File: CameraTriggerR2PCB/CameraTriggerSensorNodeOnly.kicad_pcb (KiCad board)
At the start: 2 copper layers, 73.7 x 100.3 mm, 44 parts, among them IC1 3178, J1 Power, J13 +5V Always on, J13 Serial, J14 Ext power switch, J2 Qwiic_Connector, J3 Aux out, J4 HighLowIn, J5 Laser, J6 Sensor, Q1 PN2222A, SW1 AS11CB, SW3 SW_Poll, U1 LM7805_TO220

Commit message: Add files via upload
Adding LightSensor2
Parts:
- moved H1 1.27 mm to (153.7, 127.0)
- moved H4 1.27 mm to (90.2, 127.0)
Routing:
- net +3V3: track 180.6 -> 174.4 mm
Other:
- board size 73.7 x 100.3 mm -> 73.7 x 99.1 mm
- board text added: "+3.3V"
- board text added: "+5V"
- board text added: "Gnd"
- board text added: "Sensor"
- board text removed: "+3.3"
- board text removed: "SIG"
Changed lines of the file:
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@@
   (general
     (thickness 1.6)
-    (drawings 26)
-    (tracks 262)
+    (drawings 24)
+    (tracks 261)
     (zones 0)
     (modules 44)
@@
   )
   (module MountingHole:MountingHole_3.7mm_Pad (layer F.Cu)
-    (at 90.17 128.27 270)
+    (at 90.17 127 270)
     (descr "Mounting Hole 3.7mm")
     (tags "mounting hole 3.7mm")
@@
   )
   (module MountingHole:MountingHole_3.7mm_Pad (layer F.Cu)
-    (at 153.67 128.27 270)
+    (at 153.67 127 270)
     (descr "Mounting Hole 3.7mm")
     (tags "mounting hole 3.7mm")
@@
     )
   )
-  (gr_text +5 (at 92.71 81.28) (layer F.Cu)
-    (effects (font (size 1.5 1.5) (thickness 0.3)))
-  )
-  (gr_text Rx (at 97.79 86.36) (layer F.Cu)
-    (effects (font (size 1.5 1.5) (thickness 0.3)))
-  )
-  (gr_text Tx (at 97.79 91.44) (layer F.Cu)
-    (effects (font (size 1.5 1.5) (thickness 0.3)))
-  )
-  (gr_text G (at 92.71 96.52) (layer F.Cu)
-    (effects (font (size 1.5 1.5) (thickness 0.3)))
-  )
-  (gr_text Signal (at 100.33 116.84) (layer F.Cu)
-    (effects (font (size 1.5 1.5) (thickness 0.3)))
-  )
-  (gr_text +3.3 (at 99.06 121.92) (layer F.Cu)
-    (effects (font (size 1.5 1.5) (thickness 0.3)))
-  )
-  (gr_text G (at 97.79 114.3) (layer F.Cu)
-    (effects (font (size 1.5 1.5) (thickness 0.3)))
-  )
-  (gr_text G (at 114.3 44.45) (layer F.Cu)
-    (effects (font (size 1.5 1.5) (thickness 0.3)))
-  )
-  (gr_text +5 (at 118.11 44.45) (layer F.Cu)
-    (effects (font (size 1.5 1.5) (thickness 0.3)))
-  )
-  (gr_text G (at 144.78 96.52) (layer F.Cu)
-    (effects (font (size 1.5 1.5) (thickness 0.3)))
-  )
-  (gr_text +5 (at 143.51 93.98) (layer F.Cu)
-    (effects (font (size 1.5 1.5) (thickness 0.3)))
-  )
-  (gr_text +3.3 (at 135.89 104.14) (layer F.Cu)
-    (effects (font (size 1.5 1.5) (thickness 0.3)))
-  )
-  (gr_text G (at 137.16 110.49) (layer F.Cu)
-    (effects (font (size 1.5 1.5) (thickness 0.3)))
-  )
-  (gr_text SIG (at 137.16 106.68) (layer F.Cu)
-    (effects (font (size 1.5 1.5) (thickness 0.3)))
-  )
-  (gr_text SIG (at 146.05 116.84) (layer F.Cu)
-    (effects (font (size 1.5 1.5) (thickness 0.3)))
-  )
-  (gr_text G (at 147.32 119.38) (layer F.Cu)
-    (effects (font (size 1.5 1.5) (thickness 0.3)))
-  )
+  (gr_text Gnd (at 114.3 41.91) (layer Dwgs.User)
+    (effects (font (size 1 1) (thickness 0.15)))
+  )
+  (gr_text +5V (at 118.11 41.91) (layer Dwgs.User)
+    (effects (font (size 1 1) (thickness 0.15)))
+  )
+  (gr_text G (at 95.25 96.52) (layer Dwgs.User)
+    (effects (font (size 1 1) (thickness 0.15)))
+  )
+  (gr_text +5 (at 91.44 81.28) (layer Dwgs.User)
+    (effects (font (size 1 1) (thickness 0.15)))
+  )
+  (gr_text Rx (at 96.52 86.36) (layer Dwgs.User)
+    (effects (font (size 1 1) (thickness 0.15)))
+  )
+  (gr_text Tx (at 99.06 92.71) (layer Dwgs.User)
+    (effects (font (size 1 1) (thickness 0.15)))
+  )
+  (gr_text Gnd (at 144.78 96.52) (layer Dwgs.User)
+    (effects (font (size 1 1) (thickness 0.15)))
+  )
+  (gr_text +5V (at 144.78 93.98) (layer Dwgs.User)
+    (effects (font (size 1 1) (thickness 0.15)))
+  )
+  (gr_text Gnd (at 137.16 109.22) (layer Dwgs.User)
+    (effects (font (size 1 1) (thickness 0.15)))
+  )
+  (gr_text Sensor (at 137.16 106.68) (layer Dwgs.User)
+    (effects (font (size 1 1) (thickness 0.15)))
+  )
+  (gr_text +3.3V (at 135.89 104.14) (layer Dwgs.User)
+    (effects (font (size 1 1) (thickness 0.15)))
+  )
+  (gr_text Gnd (at 146.05 119.38) (layer Dwgs.User)
+    (effects (font (size 1 1) (thickness 0.15)))
+  )
+  (gr_text Signal (at 147.32 115.57) (layer Dwgs.User)
+    (effects (font (size 1 1) (thickness 0.15)))
+  )
+  (gr_text Sensor (at 97.79 116.84) (layer Dwgs.User)
+    (effects (font (size 1 1) (thickness 0.15)))
+  )
+  (gr_text +3.3V (at 97.79 121.92) (layer Dwgs.User)
+    (effects (font (size 1 1) (thickness 0.15)))
+  )
+  (gr_text Gnd (at 97.79 114.3) (layer Dwgs.User)
+    (effects (font (size 1 1) (thickness 0.15)))
+  )
+  (dimension 99.06 (width 0.15) (layer Dwgs.User)
+    (gr_text "3.9000 in" (at 69.82 82.55 90) (layer Dwgs.User)
+      (effects (font (size 1 1) (thickness 0.15)))
+    )
+    (feature1 (pts (xy 85.09 33.02) (xy 70.533579 33.02)))
+    (feature2 (pts (xy 85.09 132.08) (xy 70.533579 132.08)))
+    (crossbar (pts (xy 71.12 132.08) (xy 71.12 33.02)))
+    (arrow1a (pts (xy 71.12 33.02) (xy 71.706421 34.146504)))
+    (arrow1b (pts (xy 71.12 33.02) (xy 70.533579 34.146504)))
+    (arrow2a (pts (xy 71.12 132.08) (xy 71.706421 130.953496)))
+    (arrow2b (pts (xy 71.12 132.08) (xy 70.533579 130.953496)))
+  )
+  (gr_line (start 85.09 132.08) (end 158.75 132.08) (layer Edge.Cuts) (width 0.1))
   (dimension 73.66 (width 0.15) (layer Dwgs.User)
     (gr_text "2.9000 in" (at 121.92 8.86) (layer Dwgs.User)
@@
   )
   (gr_line (start 85.09 33.02) (end 91.44 33.02) (layer Edge.Cuts) (width 0.1))
-  (gr_line (start 85.09 133.35) (end 91.44 133.35) (layer Edge.Cuts) (width 0.1))
-  (gr_line (start 85.09 133.35) (end 85.09 33.02) (layer Edge.Cuts) (width 0.1))
-  (gr_line (start 95.25 133.35) (end 91.44 133.35) (layer Edge.Cuts) (width 0.1))
+  (gr_line (start 85.09 132.08) (end 85.09 33.02) (layer Edge.Cuts) (width 0.1))
   (gr_line (start 91.44 33.02) (end 95.25 33.02) (layer Edge.Cuts) (width 0.1))
-  (dimension 100.33 (width 0.15) (layer Dwgs.User)
-    (gr_text "3.9500 in" (at 52.04 83.185 90) (layer Dwgs.User)
-      (effects (font (size 1 1) (thickness 0.15)))
-    )
-    (feature1 (pts (xy 72.39 33.02) (xy 52.753579 33.02)))
-    (feature2 (pts (xy 72.39 133.35) (xy 52.753579 133.35)))
-    (crossbar (pts (xy 53.34 133.35) (xy 53.34 33.02)))
-    (arrow1a (pts (xy 53.34 33.02) (xy 53.926421 34.146504)))
-    (arrow1b (pts (xy 53.34 33.02) (xy 52.753579 34.146504)))
-    (arrow2a (pts (xy 53.34 133.35) (xy 53.926421 132.223496)))
-    (arrow2b (pts (xy 53.34 133.35) (xy 52.753579 132.223496)))
-  )
   (gr_line (start 158.75 33.02) (end 95.25 33.02) (layer Edge.Cuts) (width 0.1))
-  (gr_line (start 158.75 133.35) (end 158.75 33.02) (layer Edge.Cuts) (width 0.1))
-  (gr_line (start 95.25 133.35) (end 158.75 133.35) (layer Edge.Cuts) (width 0.1))
+  (gr_line (start 158.75 132.08) (end 158.75 33.02) (layer Edge.Cuts) (width 0.1))
   (via (at 96.52 67.31) (size 0.8) (drill 0.4) (layers F.Cu B.Cu) (net 1))
   (via (at 99.06 67.31) (size 0.8) (drill 0.4) (layers F.Cu B.Cu) (net 1))
@@
   (segment (start 87.085001 82.898001) (end 87.085001 75.655001) (width 0.25) (layer B.Cu) (net 5))
   (segment (start 85.634999 84.348003) (end 87.085001 82.898001) (width 0.25) (layer B.Cu) (net 5))
-  (segment (start 86.36 124.46) (end 85.634999 123.734999) (width 0.25) (layer B.Cu) (net 5))
-  (segment (start 85.634999 123.734999) (end 85.634999 84.348003) (width 0.25) (layer B.Cu) (net 5))
   (segment (start 86.81001 75.38001) (end 93.52999 75.38001) (width 0.25) (layer B.Cu) (net 5))
   (segment (start 93.52999 75.38001) (end 95.25 73.66) (width 0.25) (layer B.Cu) (net 5))
@@
   (segment (start 97.593002 73.66) (end 99.596501 71.656501) (width 0.25) (layer B.Cu) (net 5))
   (segment (start 99.596501 71.656501) (end 102.325001 68.928001) (width 0.25) (layer B.Cu) (net 5))
-  (segment (start 87.63 124.46) (end 91.44 120.65) (width 0.25) (layer B.Cu) (net 5))
-  (segment (start 86.36 124.46) (end 87.63 124.46) (width 0.25) (layer B.Cu) (net 5))
   (segment (start 92.71 121.92) (end 91.44 120.65) (width 0.25) (layer F.Cu) (net 5))
   (segment (start 92.71 123.19) (end 92.71 121.92) (width 0.25) (layer F.Cu) (net 5))
+  (segment (start 87.63 120.65) (end 85.634999 118.654999) (width 0.25) (layer B.Cu) (net 5))
+  (segment (start 91.44 120.65) (end 87.63 120.65) (width 0.25) (layer B.Cu) (net 5))
+  (segment (start 85.634999 118.654999) (end 85.634999 84.348003) (width 0.25) (layer B.Cu) (net 5))
   (segment (start 91.44 118.11) (end 102.87 118.11) (width 0.25) (layer F.Cu) (net 6))
   (segment (start 104.14 116.84) (end 107.95 116.84) (width 0.25) (layer F.Cu) (net 6))
@@
     (polygon
       (pts
-        (xy 85.09 33.02) (xy 158.75 33.02) (xy 158.75 134.62) (xy 83.82 133.35) (xy 85.09 31.75)
+        (xy 85.09 33.02) (xy 158.75 33.02) (xy 158.75 132.08) (xy 85.09 132.08)
       )
     )

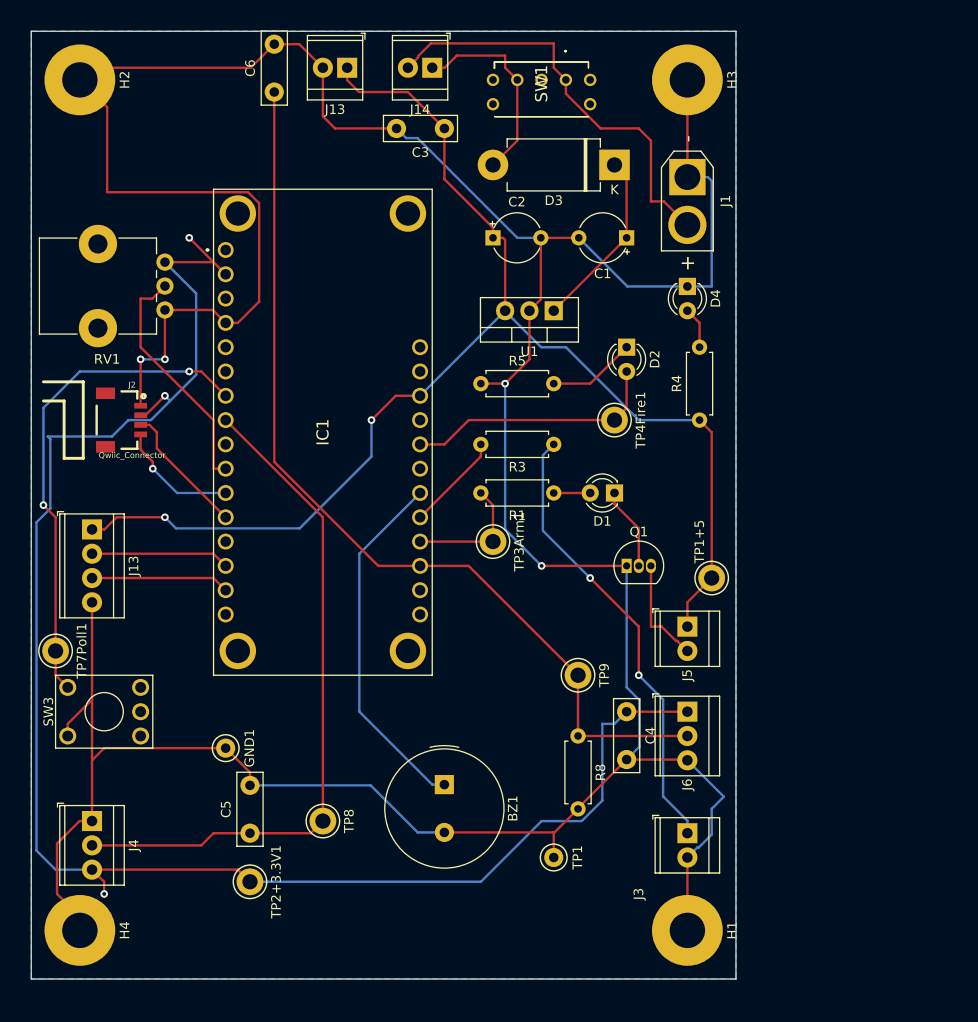
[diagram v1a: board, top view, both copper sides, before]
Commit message: Add files via upload
Rdo SCK SDL to correct pins
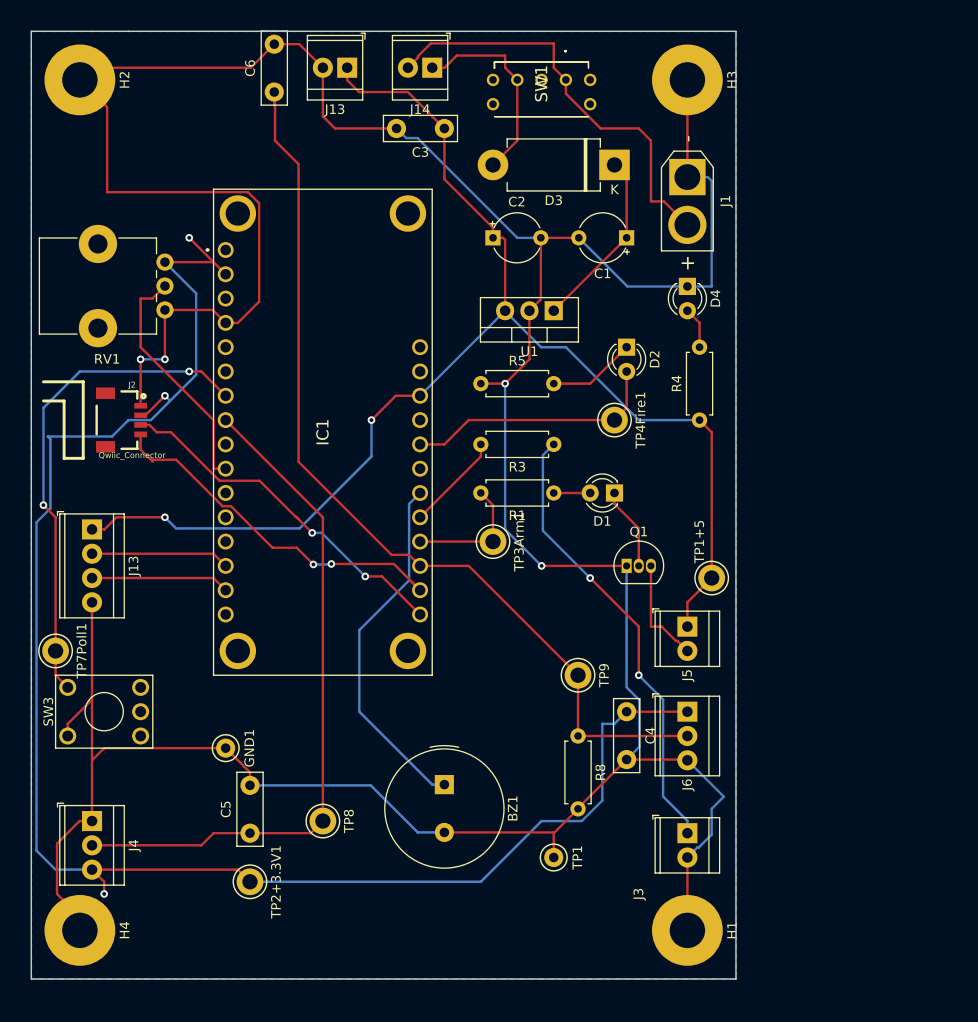
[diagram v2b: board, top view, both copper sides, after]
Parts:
- IC1: footprint SamacSys_Parts:3178 -> 3178
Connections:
- IC1 pad 11: /SCL -> SCL_qwiic
- IC1 pad 12: /SDA -> SDA_qwiic
- IC1 pad 17: SDA_qwiic -> /MOSI
- IC1 pad 18: SCL_qwiic -> /SCK
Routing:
- net SCL_qwiic: track 12.8 -> 38.4 mm, vias 1 -> 2
- net SDA_qwiic: track 13.9 -> 37.7 mm, vias 0 -> 2
- net SensorIn: track 97.4 -> 96.2 mm

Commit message: Add files via upload
Adding XLR connector
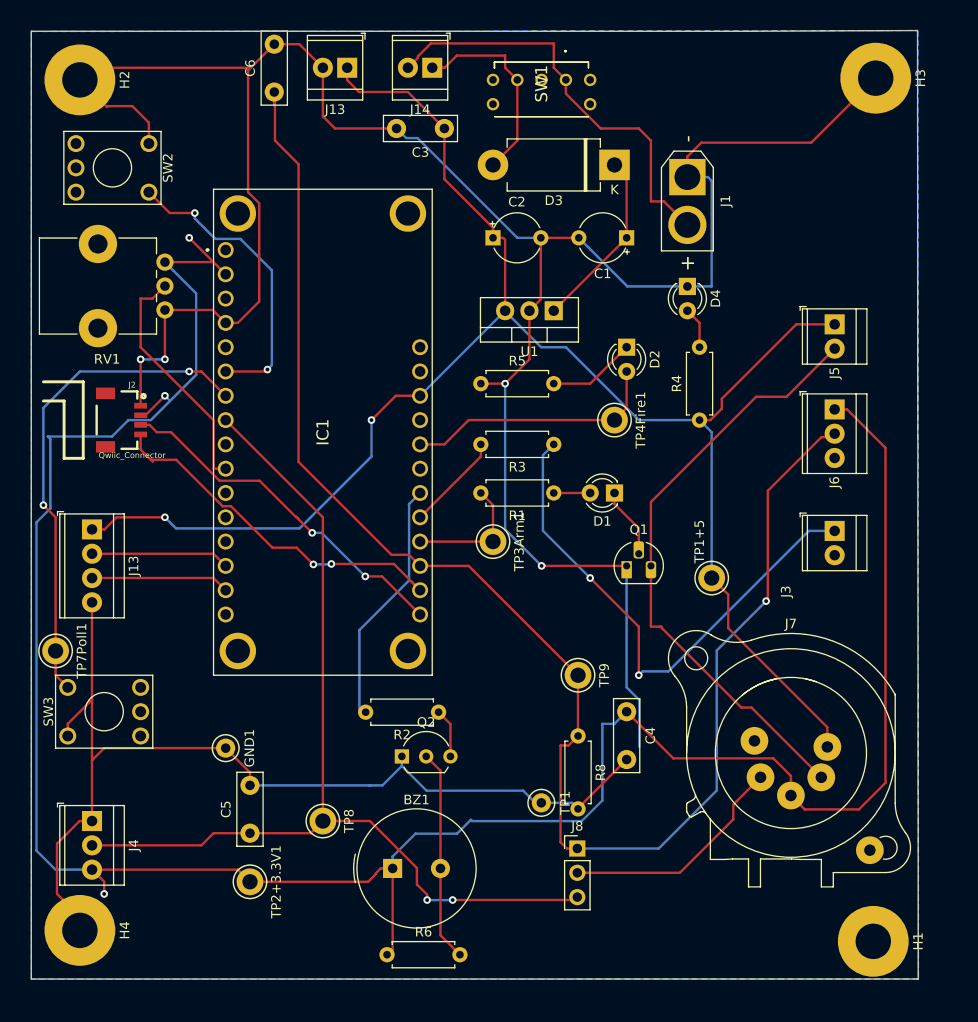
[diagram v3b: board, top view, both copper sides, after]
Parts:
- added J7: XLR5, SamacSys_Parts:Jack_XLR_Neutrik_NC5FAV-DA_Vertical, F.Cu at (168.3, 107.8)
- added J8: , Connector_PinHeader_2.54mm:PinHeader_1x03_P2.54mm_Vertical, F.Cu at (142.2, 118.4)
- added Q2: KSC1815YTA, Package_TO_SOT_THT:TO-92L_Inline_Wide, F.Cu at (123.8, 108.8)
- added R2: 1K, Resistor_THT:R_Axial_DIN0207_L6.3mm_D2.5mm_P7.62mm_Horizontal, F.Cu at (127.7, 104.2)
- added R6: 1K, Resistor_THT:R_Axial_DIN0207_L6.3mm_D2.5mm_P7.62mm_Horizontal, F.Cu at (122.3, 129.5)
- added SW2: SW_Arm, Button_Switch_THT:KSA_Tactile_SPST, F.Cu at (97.4, 44.8)
- GND1, TP1: value TestPoint -> Gnd
- H2, H3: value MountingHole_Pad -> (none)
- Q1: footprint Package_TO_SOT_THT:TO-92_Inline -> Package_TO_SOT_THT:TO-92L_HandSolder
- moved J3 35.1 mm to (169.1, 85.2)
- moved J5 35.1 mm to (169.1, 63.7)
- moved J6 35.1 mm to (169.1, 72.5)
- moved H3 19.7 mm to (173.4, 37.9)
- moved H1 19.5 mm to (173.1, 128.1)
- moved BZ1 10.3 mm to (122.9, 120.5), turned to 0 degrees
- moved TP1 5.86 mm to (138.4, 113.7)
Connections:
- net Net-(J5-Pad2) renamed Laser
- BZ1 pad 1: Buzzer -> +3V3
- BZ1 pad 2: GND -> Net-(BZ1-Pad2)
- IC1 pad 23: /A1 -> ArmIn
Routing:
- net +3V3: track 174.4 -> 253.9 mm
- net SensorIn: track 96.2 -> 159.2 mm, vias 0 -> 1
- net Laser: track 11.2 -> 63.3 mm
- net +5V: track 139.9 -> 175.3 mm
- net ArmIn: track 0.00 -> 31.6 mm, vias 0 -> 2
- net AuxIn: track 71.3 -> 102.8 mm, vias 0 -> 2
- net GND: track 384.5 -> 359.8 mm
- net Net-(J7-Pad4): track 0.00 -> 24.2 mm
- net Net-(BZ1-Pad2): track 0.00 -> 22.2 mm
- net Buzzer: track 37.5 -> 25.5 mm
- net Net-(J3-Pad1): track 47.4 -> 55.5 mm
- net Net-(Q2-Pad3): track 0.00 -> 5.14 mm
- net Net-(D1-Pad1): track 8.67 -> 7.67 mm
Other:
- board size 73.7 x 99.1 mm -> 92.7 x 99.1 mm
- board text added: "1"
- board text added: "1 +5 2 Laser 3 +3 4 Sensor 5 Gnd"
- board text added: "5"
- board text added: "HighLow"
- board text added: "HighLow Sensor"
- board text added: "LowHigh"
- board text added: "RocketTrig SensorNode Rev2B Curtis Heisey"

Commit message: Add files via upload
Production version
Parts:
- removed J8: , Connector_PinHeader_2.54mm:PinHeader_1x03_P2.54mm_Vertical
- added SW4: SW_SPDT, Button_Switch_THT:SW_Slide_1P2T_CK_OS102011MS2Q, F.Cu at (144.3, 127.0)
- GND1: value Gnd -> TestPoint
- J7: footprint SamacSys_Parts:Jack_XLR_Neutrik_NC5FAV-DA_Vertical -> SamacSys_Parts:Jack_XLR_Neutrik_NC5MBH_Horizontal
- moved J7 12.0 mm to (161.4, 117.7), turned to 90 degrees
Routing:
- net +5V: track 175.3 -> 206.6 mm
- net GND: track 359.8 -> 374.9 mm
- net Laser: track 63.3 -> 74.2 mm
- net +3V3: track 253.9 -> 243.5 mm
- net SensorIn: track 159.2 -> 166.9 mm, vias 1 -> 2
- net Net-(J7-Pad4): track 24.2 -> 30.6 mm
- net AuxIn: track 102.8 -> 106.1 mm
